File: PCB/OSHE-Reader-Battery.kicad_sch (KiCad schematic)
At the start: 15 parts, among them J4 S2B-PH-K-SLFSN, Q1 Q_PNP_BCEC, U1 BQ2057CSNTR, U2 IRF7326D2TRPBF

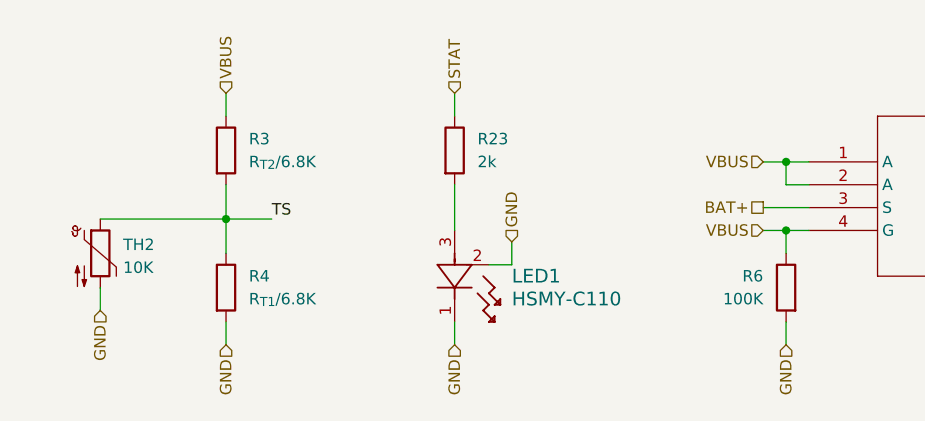
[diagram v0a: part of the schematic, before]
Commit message: Finishing touches with renaming some components and making auto BOM look cleaner
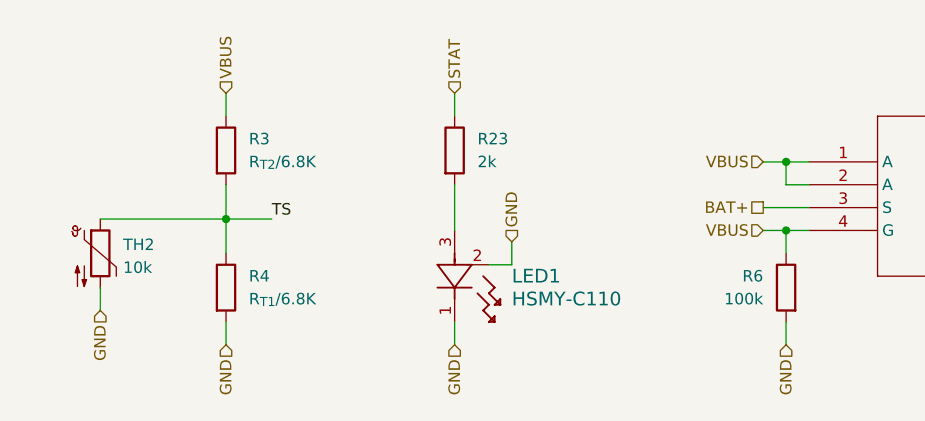
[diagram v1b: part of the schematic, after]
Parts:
- R6: value 100K -> 100k
- TH2: value 10K -> 10k
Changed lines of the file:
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@@
 			)
 		)
-		(property "Value" "10K"
+		(property "Value" "10k"
 			(at 27.94 104.4574 0)
 			(effects
@@
 			)
 		)
-		(property "Value" "100K"
+		(property "Value" "100k"
 			(at 99.06 107.9499 0)
 			(effects

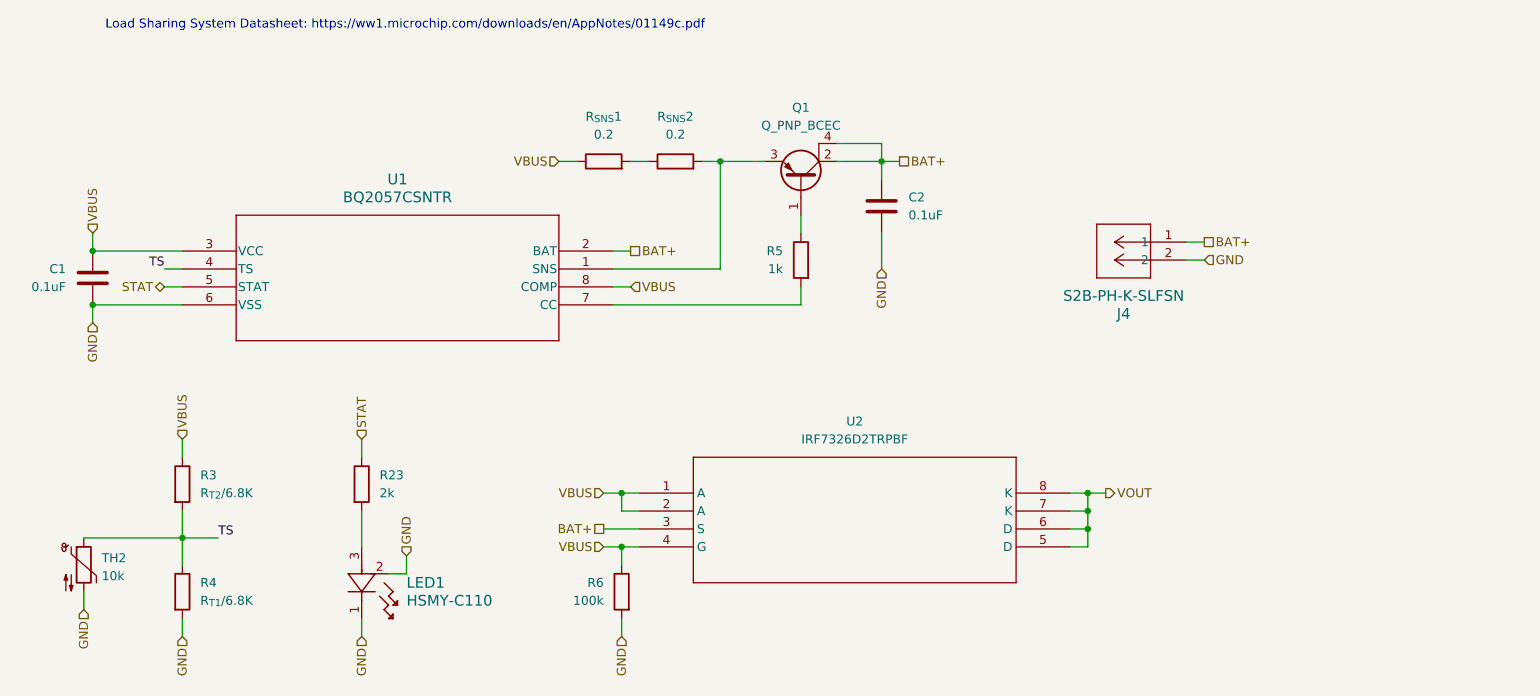
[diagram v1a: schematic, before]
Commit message: Minor fixes to PCB: schottky diode for battery charging and general battery charging routing fixes
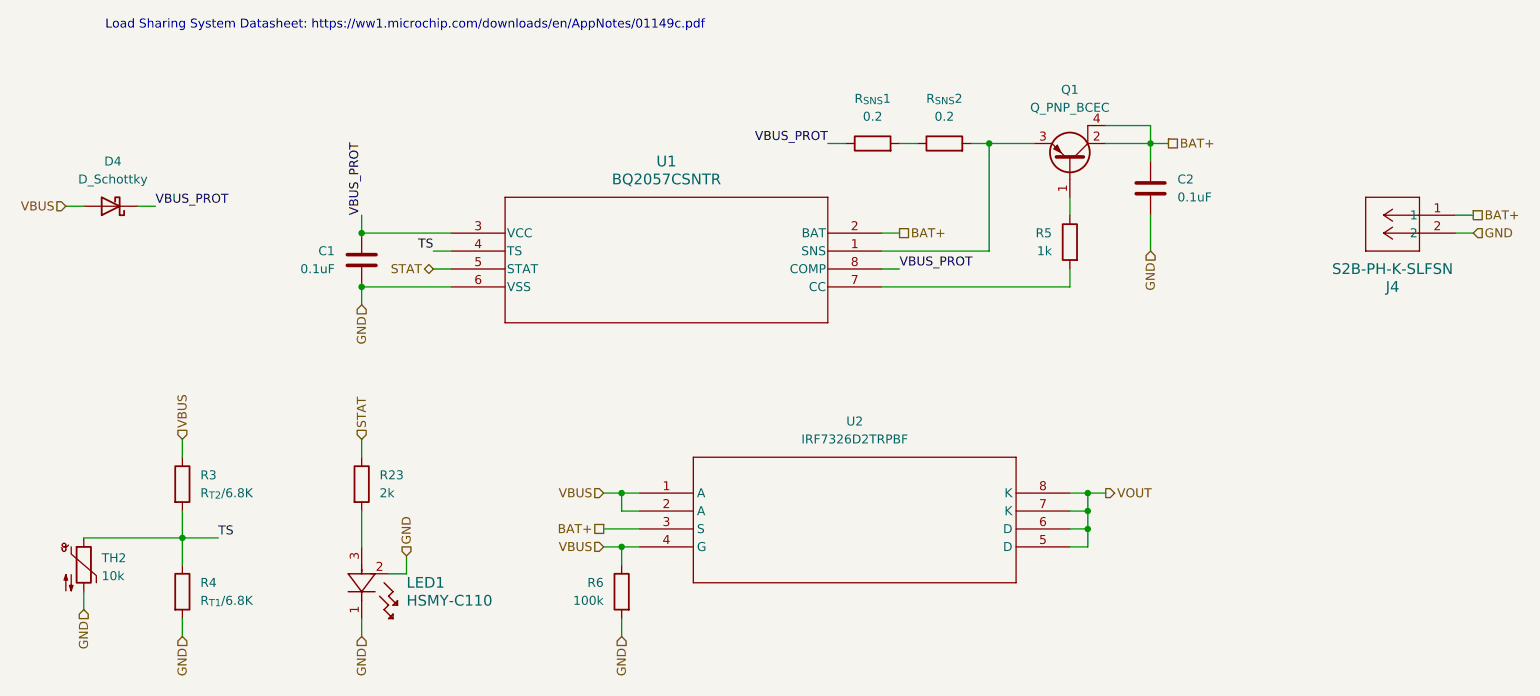
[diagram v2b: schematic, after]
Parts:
- added D4: D_Schottky, Diode_SMD:D_1206_3216Metric_Pad1.42x1.75mm_HandSolder, symbol Device:D_Schottky
- LED1: footprint LED3_HSMx-C110_AVA -> ul_HSMY-C110:LED3_HSMx-C110_AVA
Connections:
- net VBUS: now also D4.2 (A); no longer C1.1, R_{SNS}1.1, U1.3 (VCC), U1.8 (COMP)
- new net VBUS_PROT: C1.1, D4.1 (K), R_{SNS}1.1, U1.3 (VCC), U1.8 (COMP)
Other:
- moved on the sheet: C1, C2, J4, Q1, R5, R_{SNS}1, R_{SNS}2, U1
